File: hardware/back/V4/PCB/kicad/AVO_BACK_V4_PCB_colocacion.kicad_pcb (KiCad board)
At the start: 4 copper layers, 46.7 x 47.4 mm, 105 parts, among them J1 USB-C 16P, J2 BATERÍA 1S, J3 microSD DM3AT, J4 URTK1.2 (8 hilos), Q1 AO3401A, Q2 AO3401A, Q3 AO3401A, Q4 AO3401A, U1 BQ51013BRHLR, U2 BQ24072RGTR, U3 TLV75733PDBVR, U4 ESP32-S3-MINI-1U-N8, U6 USBLC6-2SC6, U7 RT9080-33GJ5, U8 DRV5032FADBZR

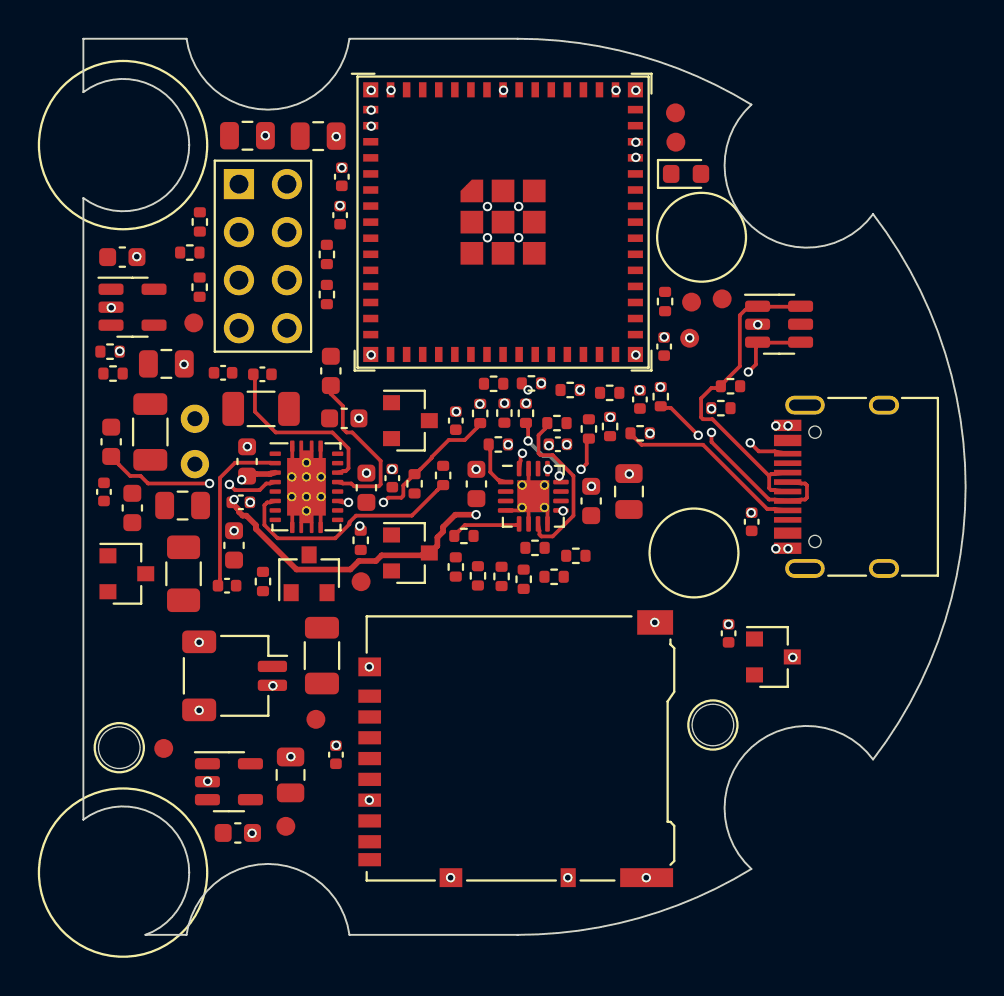
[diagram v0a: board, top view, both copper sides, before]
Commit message: PCB espalda V4: bloque Qi junto a los pines de U1, contorno con tornillos a 0,5 mm, Freerouting -mp 150
Co-Authored-By: Claude Opus 5.5 <noreply@anthropic.com>
Claude-Session: https://claude.ai/code/session_01CHDvF5XNd4qsah8Nejvp3z
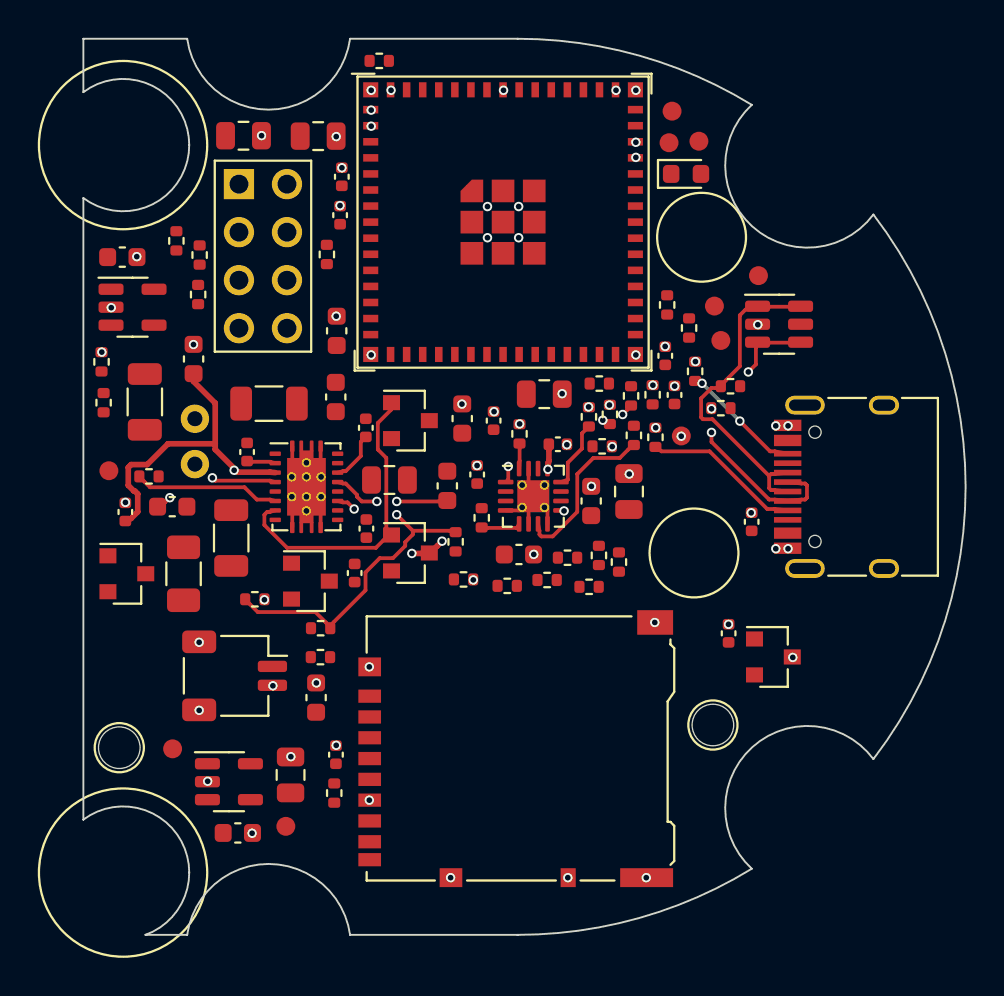
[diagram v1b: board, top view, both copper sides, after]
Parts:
- moved TP2 26.9 mm to (96.7, 81.8)
- moved TP9 22.9 mm to (99.4, 92.3)
- moved C62 20.8 mm to (90.1, 95.1)
- moved R47 17.9 mm to (79.0, 116.2), turned to 90 degrees
- moved R4 15.6 mm to (69.2, 99.5), turned to 0 degrees
- moved R2 15.5 mm to (74.8, 106.0), turned to 0 degrees
- moved TP7 15.0 mm to (67.0, 99.2)
- moved R54 14.3 mm to (81.3, 77.5)
- moved C8 14.0 mm to (80.7, 102.2)
- moved C61 12.7 mm to (74.2, 81.4)
- moved C11 12.7 mm to (80.0, 104.6), turned to 90 degrees
- moved C5 12.3 mm to (79.0, 95.2)
- moved C4 11.0 mm to (81.9, 99.6)
- moved C40 9.15 mm to (78.0, 111.2)
- moved RT1 9.06 mm to (85.8, 104.9), turned to 0 degrees
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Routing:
- net QI_ADEN: track 0.00 -> 16.2 mm
- net VIN5: track 25.6 -> 38.3 mm, vias 5 -> 4
- net QI_FOD: track 11.6 -> 19.4 mm, vias 3 -> 2
- net QI_BOOT1: track 8.98 -> 1.50 mm
- net QI_BOOT2: track 9.44 -> 2.69 mm
- net QI_CHG: track 12.7 -> 7.71 mm
- net CHG_TS: track 2.47 -> 7.34 mm, vias 0 -> 2
- net CHG_ISET: track 5.56 -> 1.33 mm, vias 2 -> 0
- net CHG_STAT: track 4.49 -> 7.20 mm
- net QI_CLAMP1: track 9.58 -> 6.89 mm
- net QI_CLAMP2: track 8.89 -> 6.26 mm, vias 0 -> 2
- net CC1: track 9.98 -> 8.34 mm
- net CHG_EN2: track 3.69 -> 2.10 mm
- net CC2: track 7.69 -> 6.42 mm
- net CHG_ILIM: track 4.07 -> 3.66 mm, vias 2 -> 0
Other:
- outline, holes or cut-outs redrawn

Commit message: PCB espalda V4: vuelve la colocación anterior; sin pre-ruteo del bloque Qi (Freerouting lo rutea entero), tiempo de Freerouting 40 min
La colocación con el bloque Qi apiñado no convergía en Freerouting (sin sesión a los 25 min).

Co-Authored-By: Claude Opus 5.5 <noreply@anthropic.com>
Claude-Session: https://claude.ai/code/session_01CHDvF5XNd4qsah8Nejvp3z
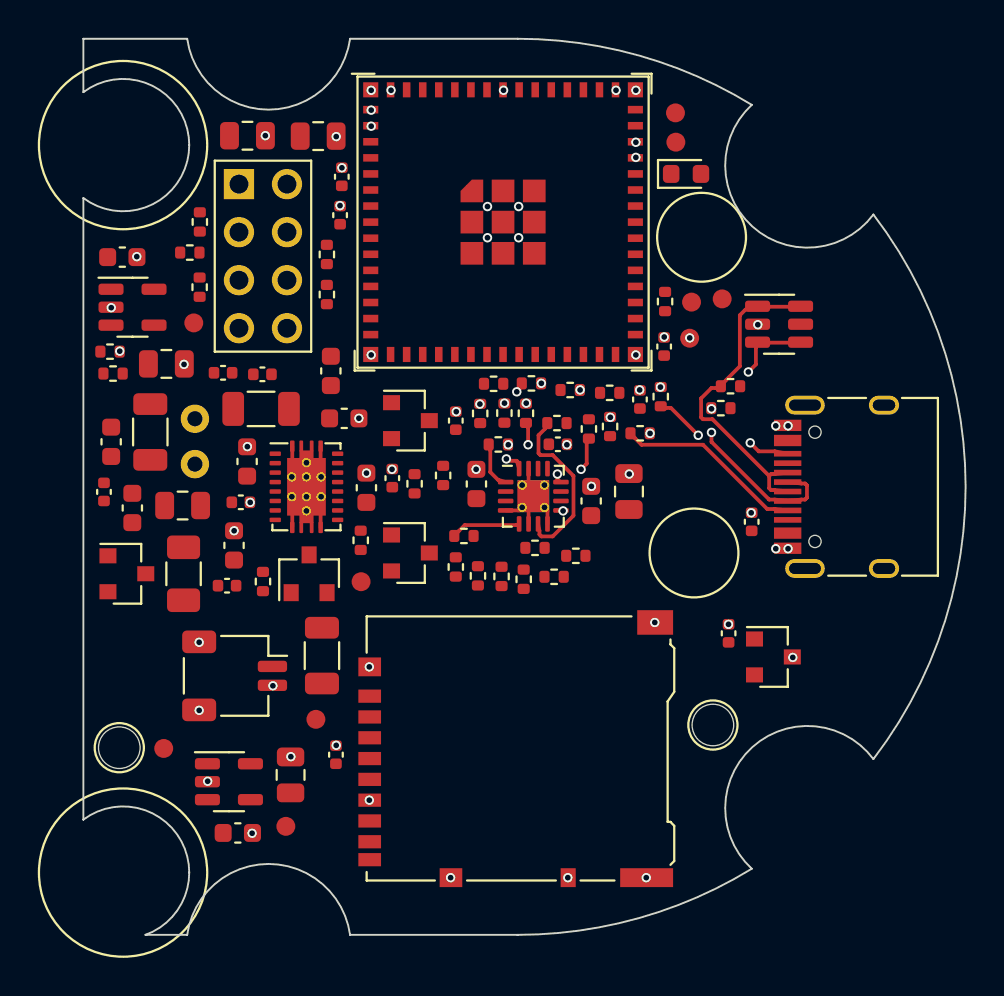
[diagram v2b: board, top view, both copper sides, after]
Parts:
- moved TP2 26.9 mm to (71.5, 91.3)
- moved TP9 22.9 mm to (80.4, 105.0)
- moved C62 20.8 mm to (74.4, 81.4)
- moved R47 17.9 mm to (91.8, 103.7), turned to 0 degrees
- moved R4 15.6 mm to (84.7, 99.4), turned to 90 degrees
- moved R2 15.5 mm to (86.7, 96.1), turned to 90 degrees
- moved TP7 15.0 mm to (70.0, 113.8)
- moved R54 14.3 mm to (71.3, 87.6)
- moved C8 14.0 mm to (66.8, 100.3)
- moved C61 12.7 mm to (70.1, 93.5)
- moved C11 12.7 mm to (73.1, 94.0), turned to 0 degrees
- moved C5 12.3 mm to (68.3, 101.1)
- moved C4 11.0 mm to (71.0, 101.0)
- moved C40 9.15 mm to (73.7, 103.1)
- moved RT1 9.06 mm to (88.0, 96.1), turned to 90 degrees
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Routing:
- net VIN5: track 38.3 -> 0.00 mm, vias 4 -> 0
- net QI_FOD: track 19.4 -> 0.00 mm, vias 2 -> 0
- net QI_ADEN: track 16.2 -> 0.00 mm
- net QI_CHG: track 7.71 -> 0.00 mm
- net QI_CLAMP1: track 6.89 -> 0.00 mm, vias 2 -> 0
- net QI_CLAMP2: track 6.26 -> 0.00 mm, vias 2 -> 0
- net CHG_TS: track 7.34 -> 2.47 mm, vias 2 -> 0
- net CHG_ISET: track 1.33 -> 5.70 mm, vias 0 -> 2
- net CHG_STAT: track 7.20 -> 4.49 mm
- net QI_BOOT2: track 2.69 -> 0.00 mm
- net CC1: track 8.34 -> 9.98 mm
- net CHG_EN2: track 2.10 -> 3.69 mm
- net QI_BOOT1: track 1.50 -> 0.00 mm
- net CC2: track 6.42 -> 7.69 mm
- net CHG_ILIM: track 3.66 -> 3.90 mm, vias 0 -> 2

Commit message: PCB espalda V4: núcleo del receptor Qi con la disposición de la cincha (U1 girado 90°, C6–C14, R1–R3, RT1) y condensadores de resonancia junto a la bobina
Con la colocación anterior Freerouting y repair.py dejaban siempre 5 pines de U1 sin unir (CLAMP, COMM, RECT, TS).

Co-Authored-By: Claude Opus 5.5 <noreply@anthropic.com>
Claude-Session: https://claude.ai/code/session_01CHDvF5XNd4qsah8Nejvp3z
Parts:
- moved C40 19.2 mm to (91.6, 96.3)
- moved TP9 17.0 mm to (67.1, 94.5)
- moved C7 15.3 mm to (78.8, 107.5), turned to 270 degrees
- moved R40 14.3 mm to (86.6, 96.4)
- moved C8 14.1 mm to (79.9, 105.4), turned to 0 degrees
- moved Q4 13.9 mm to (88.9, 96.5)
- moved C3 12.3 mm to (69.0, 101.0)
- moved TP7 11.8 mm to (66.9, 102.5)
- moved R55 11.6 mm to (78.5, 96.9), turned to 90 degrees
- moved R43 11.5 mm to (78.5, 109.7), turned to 0 degrees
- moved R41 11.1 mm to (75.6, 103.1)
- moved R53 9.59 mm to (76.7, 94.3)
- moved C11 8.54 mm to (81.5, 95.1), turned to 90 degrees
- moved R6 8.34 mm to (81.5, 97.2), turned to 90 degrees
- moved TP8 7.74 mm to (70.4, 113.9)
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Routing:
- net CHG_TS: track 2.47 -> 7.67 mm, vias 0 -> 2
- net CHG_ILIM: track 3.90 -> 0.00 mm, vias 2 -> 0
- net CHG_STAT: track 4.49 -> 8.36 mm
- net CHG_ISET: track 5.70 -> 7.94 mm, vias 2 -> 0
- net CC2: track 7.69 -> 9.23 mm
- net CHG_EN2: track 3.69 -> 4.51 mm

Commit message: PCB espalda V4: canales libres entre U1 (Qi) y sus filas de condensadores, como en la cincha
Con la colocación 7ee8318 quedaban QI_CHG y QI_COMM1 sin salida bajo U1 (C15, C16, R41 y R46 en el canal).

Co-Authored-By: Claude Opus 5.5 <noreply@anthropic.com>
Claude-Session: https://claude.ai/code/session_01CHDvF5XNd4qsah8Nejvp3z
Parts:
- moved R32 16.9 mm to (85.2, 77.5), turned to 0 degrees
- moved R6 12.9 mm to (94.3, 95.5)
- moved R42 11.2 mm to (78.3, 110.9)
- moved R4 9.60 mm to (93.1, 95.5), turned to 90 degrees
- moved R46 9.42 mm to (87.2, 104.8), turned to 90 degrees
- moved TP10 8.46 mm to (98.8, 80.8)
- moved C16 7.24 mm to (73.3, 103.8), turned to 90 degrees
- moved R41 7.09 mm to (78.4, 109.7), turned to 0 degrees
- moved R55 5.32 mm to (83.2, 94.6), turned to 0 degrees
- moved TP1 4.88 mm to (101.5, 88.7)
- moved R33 4.54 mm to (97.1, 90.2), turned to 0 degrees
- moved RT2 4.32 mm to (96.6, 91.8)
- moved R9 3.55 mm to (94.5, 100.8), turned to 0 degrees
- moved R16 3.17 mm to (96.7, 98.7), turned to 90 degrees
- moved C15 3.12 mm to (74.8, 104.4), turned to 90 degrees
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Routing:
- net CHG_TS: track 7.67 -> 15.3 mm, vias 2 -> 0
- net CHG_ILIM: track 0.00 -> 6.84 mm
- net CHG_PG: track 9.50 -> 5.63 mm
- net CC1: track 9.60 -> 7.08 mm
- net CC2: track 9.23 -> 6.90 mm
- net CHG_STAT: track 8.36 -> 6.50 mm, vias 2 -> 0
- net CHG_ISET: track 7.94 -> 9.67 mm
- net CHG_EN2: track 4.51 -> 3.26 mm

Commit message: AVO BACK V4 PCB REV B: sin Qi ni Hall; 3 contactos en el fondo (SYS y BAT en la cola, GND aparte) con TVS; REV A congelada en PCB_REV_A_QI
Soporte del chaleco = puente SYS–BAT (encendido); base de carga = cargador externo entre BAT y GND. USB-C del taller con
el BQ24072. Colocación nueva sin bloque Qi.

Co-Authored-By: Claude Opus 5.5 <noreply@anthropic.com>
Claude-Session: https://claude.ai/code/session_01CHDvF5XNd4qsah8Nejvp3z
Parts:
- removed C1, C2: 100n C0G 50V, AVO:C_1206_3216Metric
- removed C10, C7: 470n 25V, AVO:C_0603_1608Metric
- removed C11, C8: 22n 50V, AVO:C_0402_1005Metric
- removed C12, C13, C15: 10u 25V, AVO:C_0603_1608Metric
- removed C14, C16, C33: 100n, AVO:C_0402_1005Metric
- removed C17: 1u, AVO:C_0402_1005Metric
- removed C3: 47n C0G 50V, AVO:C_1206_3216Metric
- removed C4: 2n2 C0G 50V, AVO:C_0805_2012Metric
- removed C5: 1n C0G 50V, AVO:C_0603_1608Metric
- removed C6, C9: 10n 50V, AVO:C_0402_1005Metric
- removed L1: BOBINA Qi (1), AVO:WirePad_D1.5_Drill0.8
- removed L2: BOBINA Qi (2), AVO:WirePad_D1.5_Drill0.8
- removed Q1, Q2: AO3401A, AVO:SOT-23
- removed R1: 330R, AVO:R_0402_1005Metric
- removed R2: 200R, AVO:R_0402_1005Metric
- removed R3: 20k, AVO:R_0402_1005Metric
- removed R4: 100k, AVO:R_0402_1005Metric
- removed RT1: NTC 10k B3380, AVO:R_0402_1005Metric
- removed U1: BQ51013BRHLR, AVO:Texas_VQFN-RHL-20_ThermalVias
- removed U8: DRV5032FADBZR, AVO:SOT-23
- added D2: TVS 5 V, AVO:D_SOD-323, F.Cu at (99.8, 99.9)
- added D3: TVS 5 V, AVO:D_SOD-323, F.Cu at (99.8, 97.7)
- added P1: CONTACTO SYS, AVO:AVO_Contacto_M2_Tornillo, F.Cu at (101.0, 108.6)
- added P2: CONTACTO BAT, AVO:AVO_Contacto_M2_Tornillo, F.Cu at (106.8, 108.6)
- added P3: CONTACTO GND, AVO:AVO_Contacto_M2_Tornillo, F.Cu at (80.0, 100.0)
- moved Q3 25.9 mm to (93.7, 103.8), turned to 0 degrees
- moved TP7 24.3 mm to (91.1, 104.0)
- moved R32 17.4 mm to (82.3, 94.6)
- moved R47 15.9 mm to (77.8, 103.7)
- moved R33 13.6 mm to (84.7, 95.8)
- moved TP3 13.1 mm to (82.7, 96.0)
- moved C34 11.5 mm to (86.9, 96.8), turned to 0 degrees
- moved R7 10.5 mm to (85.0, 94.6), turned to 0 degrees
- moved RT2 10.0 mm to (87.3, 95.6), turned to 0 degrees
- moved R45 9.72 mm to (84.4, 99.3), turned to 0 degrees
- moved R53 9.59 mm to (71.9, 86.0)
- moved R54 9.46 mm to (76.3, 93.7)
- moved TP10 9.45 mm to (99.4, 90.2)
- moved C40 9.28 mm to (86.4, 104.0)
- moved Q4 9.07 mm to (83.8, 104.0), turned to 0 degrees
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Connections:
- C18 pad 1: VIN5 -> VBUS
- Q3 pad 3: BAT_F -> SYS_IN
- U2 pad 13: VIN5 -> VBUS
- U4 pad 36: QI_CHG -> unconnected-(U4-IO40-Pad36)
- U4 pad 5: HALL -> unconnected-(U4-IO1-Pad5)
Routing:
- net CHG_TS: track 15.3 -> 4.65 mm, vias 0 -> 2
- net CC1: track 7.08 -> 12.4 mm
- net CHG_ILIM: track 6.84 -> 12.0 mm
- net CHG_ISET: track 9.67 -> 4.56 mm, vias 0 -> 2
- net CHG_PG: track 5.63 -> 8.82 mm
- net GND: track 8.78 -> 5.62 mm, vias 67 -> 59
- net CHG_EN2: track 3.26 -> 5.65 mm, vias 0 -> 2
- net CC2: track 6.90 -> 8.92 mm
- net USB_DM_C: track 16.7 -> 17.5 mm, vias 3 -> 2
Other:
- board text added: "AVO BACK V4 · REV B · ESP32-S3 · 2026-10-30"
- board text added: "BAT"
- board text added: "GND"
- board text added: "SYS"
- board text removed: "AVO BACK V4 · REV A · ESP32-S3 · 2026-10-29"
- board text removed: "BOBINA Qi DEBAJO"
